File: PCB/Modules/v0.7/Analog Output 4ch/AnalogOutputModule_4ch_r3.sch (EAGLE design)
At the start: 40 parts, among them IC1 SN65HVD31DR, IC2 SN65HVD31DR, IC3 AD5754RBREZ, IC4 REF193GSZ

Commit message: -Updated analog output module PCB design
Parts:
- C13, C15, C3, C6, C8: value 0.1uf -> 0.1uF; device SparkFun-Capacitors:CAP0603-CAP -> SparkFun-Capacitors:1.0UF-0805-25V-10%
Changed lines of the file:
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@@
 <setting verticaltext="up"/>
 </settings>
-<grid distance="0.05" unitdist="inch" unit="inch" style="lines" multiple="1" display="no" altdistance="0.01" altunitdist="inch" altunit="inch"/>
+<grid distance="0.1" unitdist="inch" unit="inch" style="lines" multiple="1" display="no" altdistance="0.01" altunitdist="inch" altunit="inch"/>
 <layers>
 <layer number="1" name="Top" color="4" fill="1" visible="no" active="no"/>
@@
 <part name="GND25" library="SparkFun" deviceset="GND" device=""/>
 <part name="C4" library="SparkFun-Capacitors" deviceset="CAP" device="1206" value="10uf"/>
-<part name="C3" library="SparkFun-Capacitors" deviceset="CAP" device="0603-CAP" value="0.1uf"/>
+<part name="C3" library="SparkFun-Capacitors" deviceset="1.0UF" device="-0805-25V-10%" value="0.1uF"/>
 <part name="C5" library="SparkFun-Capacitors" deviceset="CAP" device="1206" value="10uf"/>
-<part name="C6" library="SparkFun-Capacitors" deviceset="CAP" device="0603-CAP" value="0.1uf"/>
+<part name="C6" library="SparkFun-Capacitors" deviceset="1.0UF" device="-0805-25V-10%" value="0.1uF"/>
 <part name="C7" library="SparkFun-Capacitors" deviceset="CAP" device="1206" value="10uf"/>
-<part name="C8" library="SparkFun-Capacitors" deviceset="CAP" device="0603-CAP" value="0.1uf"/>
+<part name="C8" library="SparkFun-Capacitors" deviceset="1.0UF" device="-0805-25V-10%" value="0.1uF"/>
 <part name="U$6" library="Joshparts2" deviceset="GNDPLANESHRT" device=""/>
 <part name="C9" library="SparkFun-Capacitors" deviceset="CAP" device="1206" value="4.7uf"/>
@@
 <part name="GND3" library="SparkFun-PowerSymbols" deviceset="GND" device=""/>
 <part name="C12" library="SparkFun-Capacitors" deviceset="CAP" device="1206" value="10uf"/>
-<part name="C13" library="SparkFun-Capacitors" deviceset="CAP" device="0603-CAP" value="0.1uf"/>
+<part name="C13" library="SparkFun-Capacitors" deviceset="1.0UF" device="-0805-25V-10%" value="0.1uF"/>
 <part name="GND4" library="SparkFun" deviceset="GND" device=""/>
 <part name="C14" library="SparkFun-Capacitors" deviceset="CAP" device="1206" value="1uf"/>
-<part name="C15" library="SparkFun-Capacitors" deviceset="CAP" device="0603-CAP" value="0.1uf"/>
+<part name="C15" library="SparkFun-Capacitors" deviceset="1.0UF" device="-0805-25V-10%" value="0.1uF"/>
 <part name="FRAME2" library="frames" deviceset="FRAME_B_L" device=""/>
 <part name="GND5" library="SparkFun" deviceset="GND" device=""/>

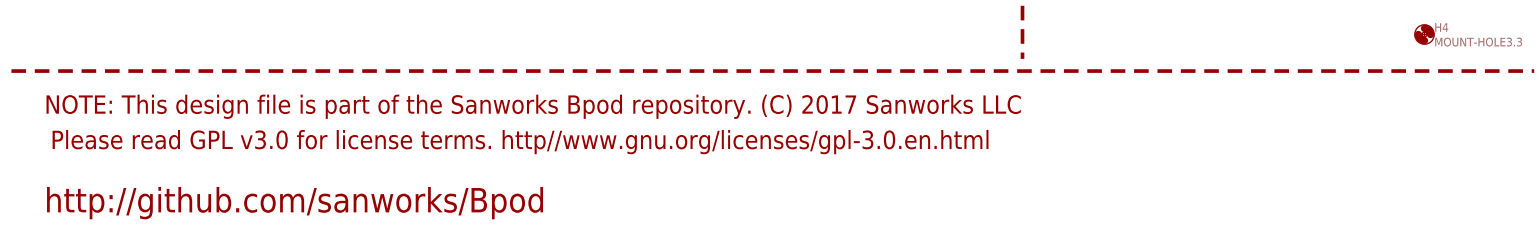
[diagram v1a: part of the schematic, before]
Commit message: -Added SNES Module PCB design -Added SNES Module bottom-guard design -Added DDS Module enclosure -Updated link to Bpod-CAD repository in schematic files
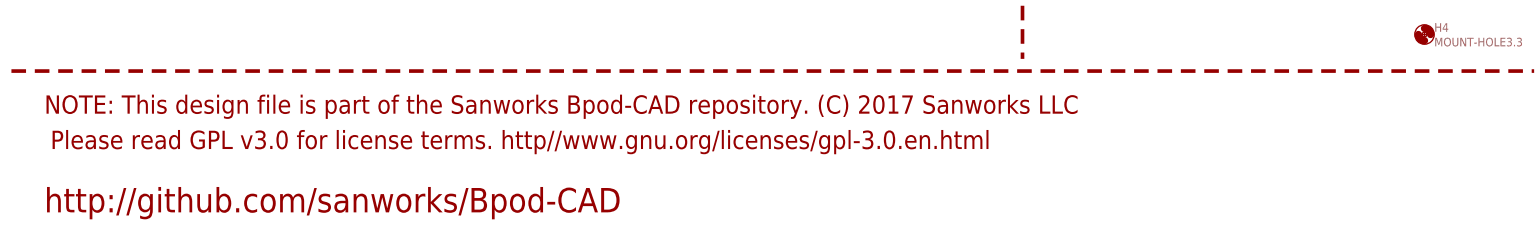
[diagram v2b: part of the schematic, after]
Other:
- note added: "NOTE: This design file is part of the Sanworks Bpod-CAD repository. (C) 2017 Sanworks LLC"
- note added: "http://github.com/sanworks/Bpod-CAD"
- note removed: "NOTE: This design file is part of the Sanworks Bpod repository. (C) 2017 Sanworks LLC"
- note removed: "http://github.com/sanworks/Bpod"
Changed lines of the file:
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@@
 <text x="180.34" y="-53.34" size="5.08" layer="94" font="vector">Ground plane bridge</text>
 <text x="-88.392" y="-150.876" size="3.81" layer="94" font="vector">Please read GPL v3.0 for license terms. http//www.gnu.org/licenses/gpl-3.0.en.html</text>
-<text x="-89.662" y="-143.51" size="3.81" layer="94" font="vector">NOTE: This design file is part of the Sanworks Bpod repository. (C) 2017 Sanworks LLC</text>
+<text x="-89.662" y="-143.51" size="3.81" layer="94" font="vector">NOTE: This design file is part of the Sanworks Bpod-CAD repository. (C) 2017 Sanworks LLC</text>
 <text x="228.6" y="-143.51" size="5.08" layer="94" font="vector">Sanworks LLC</text>
-<text x="-89.662" y="-164.084" size="5.08" layer="94" font="vector">http://github.com/sanworks/Bpod</text>
+<text x="-89.662" y="-164.084" size="5.08" layer="94" font="vector">http://github.com/sanworks/Bpod-CAD</text>
 <wire x1="-96.52" y1="-134.62" x2="220.98" y2="-134.62" width="0.762" layer="94" style="longdash"/>
 </plain>
